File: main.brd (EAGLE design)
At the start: 57.5 x 220 mm, 74 parts, among them IC10 FGPMMOPA6H, IC2 25LC1024-I/P, IC6 MPL3115A2LGA, IC7 FXAS21000, IC8 ADXL343BCCZ, Q1 12MHz, Q2 MCP9700A-E/TO, Q3 FQP7P06, Q4 MCP9700A-E/TO, U1 ATMEGA1284P-PU, U2 LT3570EFEPBF, U3 TL431BQLP, X1 132134RP

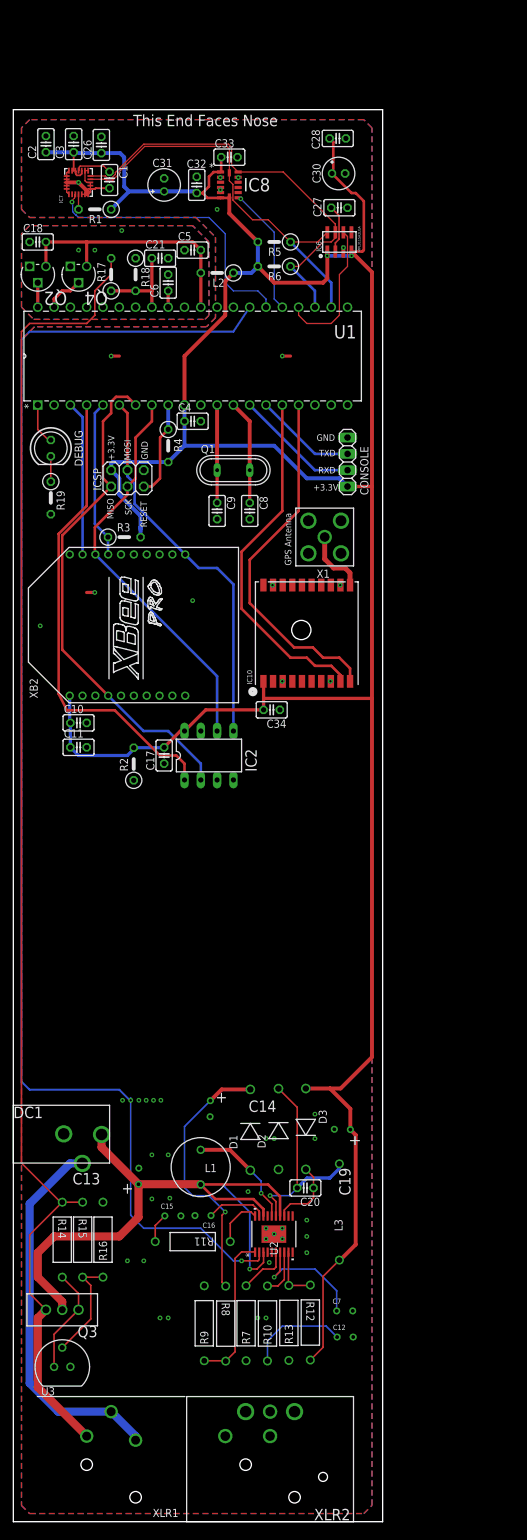
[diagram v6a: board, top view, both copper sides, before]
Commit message: Finished Power bank
Finished Power bank.
To do:
Key switch
Short circuit protection (PTCs)
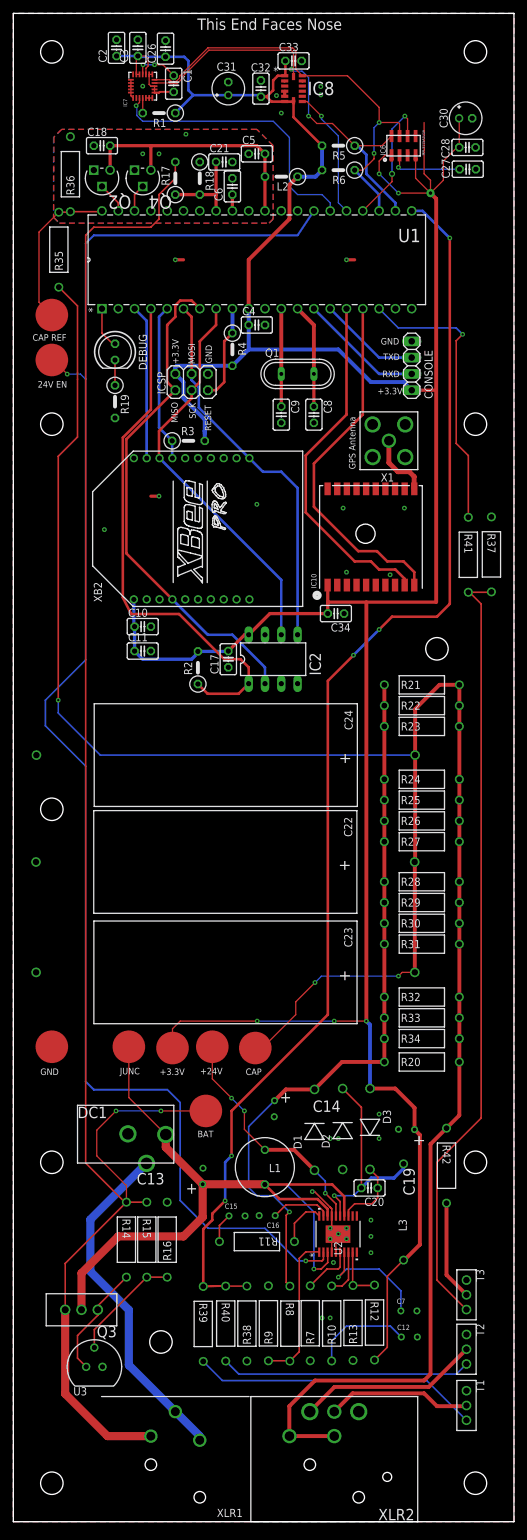
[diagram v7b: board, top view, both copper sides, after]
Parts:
- added C22, C23, C24: 338TTA035M, Power:338TTA035M
- added R20, R21, R22, R23, R24, R25, R26, R27, R28, R29, R30, R31, R32, R33, R34: 750, Power:YAG_MF25
- added R35, R36: (no value), Power:YAG_MF25
- added R37, R38: 1M, Power:YAG_MF25
- added R39, R40, R41: 3.6k, Power:YAG_MF25
- added R42: ~1.4k, Power:YAG_MF25
- added T1, T2, T3: (no value), Power:NPNDARL
- added U$1: +3.3V, Power:TEST
- added U$10, U$9: TEST, Power:TEST
- added U$2: +24V, Power:TEST
- added U$3, U$6: BAT+, Power:TEST
- added U$4, U$5: CAP, Power:TEST
- moved C30 21.6 mm to (70.5, 218.7)
- moved C27 20.9 mm to (70.8, 210.7)
- moved C28 20.2 mm to (70.7, 214.1)
- moved C2 18.6 mm to (16.1, 229.6)
- moved C10 18.0 mm to (20.2, 139.5)
- moved C1 18.0 mm to (25.0, 224.0)
- moved C11 18.0 mm to (20.2, 135.7)
- moved C18 18.0 mm to (13.8, 214.4)
- moved C21 18.0 mm to (32.9, 211.8)
- moved C26 18.0 mm to (23.7, 229.5)
- moved C3 18.0 mm to (19.4, 229.6)
- moved C32 18.0 mm to (38.6, 223.3)
- moved C33 18.0 mm to (43.7, 227.6)
- moved C6 18.0 mm to (34.1, 208.0)
- moved C8 18.0 mm to (46.8, 172.5)
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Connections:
- new net CAP_DISCHARGE: R41.1, U1.18
- new net CAP_REF: R35.2, R36.1, U$9.P$1, U1.40
- new net N$75: R42.2, T3.2
- new net N$77: T1.2, XLR2.2
- new net N$78: T2.2, XLR2.4
- new net N$79: R39.2, T1.3
- new net N$80: R40.2, T2.3
- new net N$81: C22.+, C23.+, C24.+, R20.2, R21.2, R22.2, R23.2, R24.2, R25.2, R26.2, R27.2, R28.2, R29.2, R30.2, R31.2, R32.2, R33.2, R34.2, R35.1, R42.1, U$4.P$1, XLR2.1, XLR2.3
- new net N$82: R37.2, R41.2, T3.3
- net +12.0: now also R20.1, R21.1, R22.1, R23.1, R24.1, R25.1, R26.1, R27.1, R28.1, R29.1, R30.1, R31.1, R32.1, R33.1, R34.1
- net 12V_ENABLE: now also U$10.P$1
- net A_GND: now also R36.2
- net BAT+: now also U$6.P$1
- net GND: now also C22.-, C23.-, C24.-, R37.1, R38.1, T1.1, T2.1, T3.1, U$5.P$1
- net MAIN_TRIGGER: now also R38.2, R39.1, R40.1
- net N$8: now also U$2.P$1
- net PWR_JUNC: now also U$3.P$1
- net TEMP: now also U1.39; no longer U1.40
- net TEMP2: now also U1.38; no longer U1.39
- net VCC: now also U$1.P$1
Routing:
- net N$81: track 0.00 -> 352.5 mm, vias 0 -> 3
- net MAIN_TRIGGER: track 0.00 -> 201.6 mm, vias 0 -> 5
- net N$82: track 0.00 -> 121.2 mm
- net +12.0: track 42.1 -> 113.5 mm
- net BAT+: track 207.2 -> 260.2 mm, vias 0 -> 2
- net N$79: track 0.00 -> 44.8 mm
- net CAP_DISCHARGE: track 0.00 -> 44.4 mm, vias 0 -> 1
- net VCC: track 449.4 -> 491.7 mm, vias 2 -> 6
- net N$80: track 0.00 -> 39.0 mm
- net N$78: track 0.00 -> 28.4 mm
- net CAP_REF: track 0.00 -> 24.9 mm
- net 12V_ENABLE: track 214.4 -> 239.2 mm
- net N$77: track 0.00 -> 22.6 mm
- net N$8: track 17.6 -> 37.0 mm, vias 1 -> 3
- net PWR_JUNC: track 104.6 -> 120.3 mm
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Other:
- board size 57.5 x 220 mm -> 78 x 235 mm
- board text added: "+24V"
- board text added: "24V EN"
- board text added: "BAT"
- board text added: "CAP"
- board text added: "CAP REF"
- board text added: "JUNC"

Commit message: Added more
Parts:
- moved DC1 10.0 mm to (0.00, 55.9)
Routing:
- net N$81: track 352.5 -> 363.2 mm
- net PWR_JUNC: track 120.3 -> 128.6 mm
- net N$30: track 53.8 -> 50.7 mm
- net BAT+: track 260.2 -> 259.5 mm
- net GND: vias 30 -> 38
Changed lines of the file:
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@@
 <text x="53.307" y="163.971" size="1.016" layer="25" rot="R90">GPS Antenna</text>
 <hole x="6" y="6" drill="3.5"/>
-<hole x="6" y="56" drill="3.5"/>
+<hole x="6" y="51" drill="3.5"/>
 <hole x="6" y="111" drill="3.5"/>
 <hole x="6" y="171" drill="3.5"/>
@@
 <attribute name="VENDOR" value="Texas Instruments" x="13.89" y="24.13" size="1.778" layer="27" display="off"/>
 </element>
-<element name="DC1" library="Power" package="DC_JACK_3" value="PJ-102BH" x="10" y="55.88"/>
+<element name="DC1" library="Power" package="DC_JACK_3" value="PJ-102BH" x="0" y="55.88"/>
 <element name="C20" library="rcl" library_urn="urn:adsk.eagle:library:334" package="C025-025X050" package3d_urn="urn:adsk.eagle:package:23629/2" value="0.1µF" x="55.5" y="52" rot="R180"/>
 <element name="ICSP" library="pinhead" library_urn="urn:adsk.eagle:library:325" package="2X03" package3d_urn="urn:adsk.eagle:package:22462/2" value="" x="27.78" y="177.56" smashed="yes">
@@
 <contactref element="Q3" pad="2"/>
 <contactref element="DC1" pad="1"/>
-<wire x1="23.75" y1="60.33" x2="23.75" y2="58.331" width="1.27" layer="1"/>
-<wire x1="23.75" y1="58.331" x2="29.5012" y2="52.5798" width="1.27" layer="1"/>
 <wire x1="16.35" y1="44.45" x2="26.51" y2="44.45" width="1.27" layer="1"/>
 <wire x1="26.51" y1="44.45" x2="29.5012" y2="47.4412" width="1.27" layer="1"/>
@@
 <wire x1="10.62" y1="38.72" x2="16.35" y2="44.45" width="1.27" layer="1"/>
 <contactref element="U$3" pad="P$1"/>
-<wire x1="23.75" y1="60.33" x2="18" y2="66.08" width="0.2032" layer="1"/>
-<wire x1="18" y1="66.08" x2="18" y2="74" width="0.2032" layer="1"/>
+<wire x1="18" y1="74" x2="18" y2="66.08" width="0.2032" layer="1"/>
+<wire x1="21.751" y1="60.33" x2="13.75" y2="60.33" width="1.27" layer="1"/>
+<wire x1="29.5012" y1="52.5798" x2="21.751" y2="60.33" width="1.27" layer="1"/>
+<wire x1="18" y1="66.08" x2="18" y2="64.58" width="0.254" layer="1"/>
+<wire x1="18" y1="64.58" x2="13.75" y2="60.33" width="0.254" layer="1"/>
 </signal>
 <signal name="N$6">
@@
 <contactref element="XLR1" pad="2"/>
 <wire x1="20.795" y1="49.784" x2="17.62" y2="49.784" width="0.254" layer="1"/>
-<wire x1="17.493" y1="49.657" x2="17.62" y2="49.784" width="0.254" layer="1"/>
 <contactref element="R17" pad="2"/>
 <wire x1="11.27" y1="200.42" x2="12.54" y2="201.69" width="0.254" layer="1"/>
-<wire x1="11.27" y1="200.42" x2="11.27" y2="55.88" width="0.254" layer="1"/>
-<wire x1="11.27" y1="55.88" x2="17.493" y2="49.657" width="0.254" layer="1"/>
+<wire x1="11.27" y1="200.42" x2="11.27" y2="66.73" width="0.254" layer="1"/>
 <wire x1="22.7" y1="206.77" x2="25.24" y2="209.31" width="0.254" layer="1"/>
 <wire x1="25.24" y1="209.31" x2="25.24" y2="211.85" width="0.254" layer="1"/>
@@
 <wire x1="8.08" y1="19.92" x2="8.08" y2="33.02" width="1.27" layer="1"/>
 <wire x1="14.665" y1="13.335" x2="8.08" y2="19.92" width="1.27" layer="1"/>
-<wire x1="8.08" y1="33.02" x2="8.08" y2="40.244" width="0.254" layer="1"/>
-<wire x1="8.08" y1="40.244" x2="17.493" y2="49.657" width="0.254" layer="1"/>
 <contactref element="U$6" pad="P$1"/>
-<wire x1="17.62" y1="49.784" x2="17.62" y2="52.38" width="0.2032" layer="1"/>
-<wire x1="17.62" y1="52.38" x2="13" y2="57" width="0.2032" layer="1"/>
-<wire x1="13" y1="57" x2="13" y2="61" width="0.2032" layer="1"/>
-<wire x1="13" y1="61" x2="16" y2="64" width="0.2032" layer="1"/>
-<via x="16" y="64" extent="1-16" drill="0.35"/>
-<wire x1="16" y1="64" x2="23" y2="64" width="0.2032" layer="16"/>
 <via x="23" y="64" extent="1-16" drill="0.35"/>
 <wire x1="23" y1="64" x2="30" y2="64" width="0.2032" layer="1"/>
+<wire x1="8.08" y1="33.02" x2="8.08" y2="38.08" width="0.254" layer="1"/>
+<wire x1="8.08" y1="38.08" x2="16" y2="46" width="0.254" layer="1"/>
+<wire x1="16" y1="46" x2="16" y2="48.164" width="0.254" layer="1"/>
+<wire x1="16" y1="48.164" x2="17.62" y2="49.784" width="0.254" layer="1"/>
+<wire x1="23" y1="64" x2="14" y2="64" width="0.254" layer="16"/>
+<via x="14" y="64" extent="1-16" drill="0.35"/>
+<wire x1="14" y1="64" x2="7" y2="64" width="0.254" layer="1"/>
+<wire x1="7" y1="64" x2="5" y2="62" width="0.254" layer="1"/>
+<wire x1="12.216" y1="49.784" x2="17.62" y2="49.784" width="0.254" layer="1"/>
+<wire x1="5" y1="62" x2="5" y2="57" width="0.254" layer="1"/>
+<wire x1="5" y1="57" x2="12.216" y2="49.784" width="0.254" layer="1"/>
+<wire x1="14" y1="64" x2="11.27" y2="66.73" width="0.254" layer="1"/>
 </signal>
 <signal name="N$69">
@@
 <wire x1="29.05" y1="13.34" x2="25.24" y2="17.15" width="1.27" layer="16"/>
 <wire x1="25.24" y1="17.15" x2="18" y2="24.39" width="1.27" layer="16"/>
-<wire x1="18" y1="33" x2="12" y2="39" width="1.27" layer="16"/>
-<wire x1="12" y1="47.08" x2="20.75" y2="55.83" width="1.27" layer="16"/>
 <wire x1="18" y1="24.39" x2="18" y2="33" width="1.27" layer="16"/>
-<wire x1="12" y1="39" x2="12" y2="47.08" width="1.27" layer="16"/>
+<wire x1="10.75" y1="40.25" x2="10.75" y2="55.83" width="1.27" layer="16"/>
+<wire x1="18" y1="33" x2="10.75" y2="40.25" width="1.27" layer="16"/>
 </signal>
 <signal name="12V_ENABLE">
@@
 <wire x1="50.26488125" y1="43.73511875" x2="50" y2="44" width="0.2032" layer="1"/>
 <contactref element="U$5" pad="P$1"/>
+<via x="7.4" y="66.4" extent="1-16" drill="0.35"/>
+<via x="3.5" y="59.9" extent="1-16" drill="0.35"/>
+<via x="6.1" y="58" extent="1-16" drill="0.35"/>
+<via x="9.8" y="62.7" extent="1-16" drill="0.35"/>
+<via x="18.7" y="61.9" extent="1-16" drill="0.35"/>
+<via x="20.4" y="65.6" extent="1-16" drill="0.35"/>
+<via x="21.1" y="69.8" extent="1-16" drill="0.35"/>
+<via x="29.8" y="58.7" extent="1-16" drill="0.35"/>
 </signal>
 <signal name="N$73">
@@
 <wire x1="69.49" y1="78.51" x2="69.49" y2="81.75" width="0.6096" layer="1"/>
 <wire x1="69.49" y1="81.75" x2="69.49" y2="89.99" width="0.6096" layer="1"/>
-<wire x1="69.49" y1="130.39" x2="66.39" y2="130.39" width="0.6096" layer="1"/>
-<wire x1="62.6" y1="126.6" x2="62.6" y2="119.44" width="0.6096" layer="1"/>
-<wire x1="66.39" y1="130.39" x2="62.6" y2="126.6" width="0.6096" layer="1"/>
 <wire x1="62.6" y1="119.44" x2="62.6" y2="102.86" width="0.6096" layer="1"/>
 <wire x1="62.6" y1="102.86" x2="62.53" y2="102.79" width="0.6096" layer="1"/>
@@
 <wire x1="7" y1="128" x2="7" y2="166" width="0.254" layer="1"/>
 <wire x1="7" y1="166" x2="10" y2="169" width="0.254" layer="1"/>
-<wire x1="10" y1="169" x2="10" y2="178" width="0.254" layer="1"/>
-<wire x1="10" y1="178" x2="10" y2="179" width="0.254" layer="1"/>
-<wire x1="10" y1="179" x2="10" y2="189.436" width="0.254" layer="1"/>
+<wire x1="10" y1="169" x2="10" y2="189.436" width="0.254" layer="1"/>
 <wire x1="10" y1="189.436" x2="7.09" y2="192.346" width="0.254" layer="1"/>
 <contactref element="U$4" pad="P$1"/>
@@
 <wire x1="44" y1="79" x2="38.8" y2="73.8" width="0.2032" layer="1"/>
 <wire x1="38.8" y1="73.8" x2="37.7" y2="73.8" width="0.2032" layer="1"/>
+<wire x1="62.55" y1="70.45" x2="62.55" y2="85.59" width="0.6096" layer="1"/>
+<wire x1="67.49" y1="61.314" x2="66" y2="62.804" width="0.6096" layer="1"/>
+<wire x1="66" y1="62.804" x2="66" y2="67" width="0.6096" layer="1"/>
+<wire x1="66" y1="67" x2="62.55" y2="70.45" width="0.6096" layer="1"/>
 </signal>
 <signal name="CAP_REF">
@@
 <wire x1="67.49" y1="38.46" x2="70.6" y2="35.35" width="0.6096" layer="1"/>
 </signal>
+<signal name="N$84">
+<via x="34.7" y="69.2" extent="1-16" drill="0.35"/>
+</signal>
 </signals>
